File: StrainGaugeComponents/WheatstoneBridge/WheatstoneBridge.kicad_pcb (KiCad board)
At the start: 2 copper layers, 19 x 14.5 mm, 5 parts, among them J1 Conn_01x04_Pin, J2 Conn_01x02_Pin

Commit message: Added graphics
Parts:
- renumbered J2 to INPUT
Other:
- board text added: "Pack motorsports Baja SAE Wheatstone Bdg REV1.1"
- board text added: "V+ E+ E-GND"

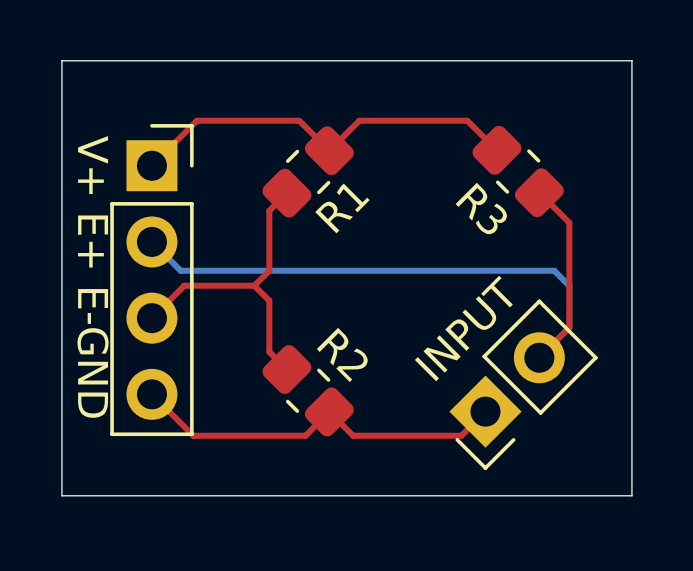
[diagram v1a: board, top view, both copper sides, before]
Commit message: Added pinout graphics
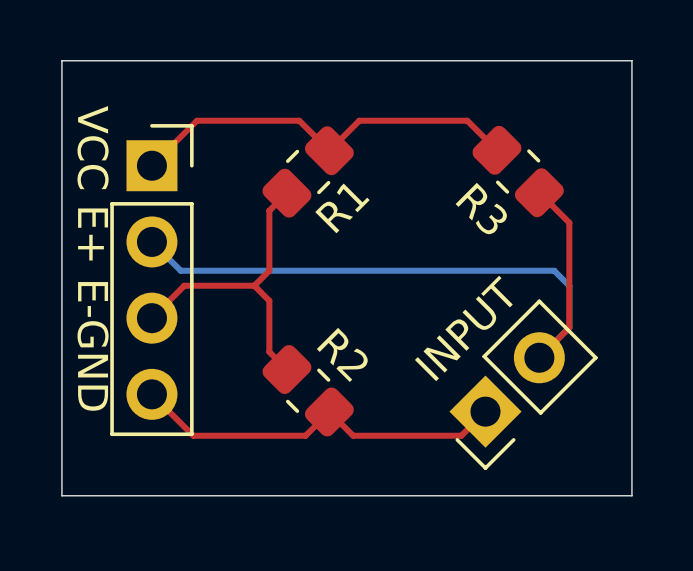
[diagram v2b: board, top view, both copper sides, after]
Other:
- board text added: "VCC E+ E-GND"
- board text removed: "V+ E+ E-GND"
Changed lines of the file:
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@@
 		)
 	)
-	(gr_text "V+ E+ E-GND"
-		(at 131.5 75.5 270)
+	(gr_text "VCC E+ E-GND"
+		(at 131.5 74.5 270)
 		(layer "F.SilkS")
 		(effects
